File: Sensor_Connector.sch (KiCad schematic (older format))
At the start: 6 parts, among them J3 Sensor_Conn

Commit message: Misc. TODOs
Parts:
- C18, C19: footprint Capacitor_SMD:C_0603_1608Metric_Pad1.05x0.95mm_HandSolder -> Capacitor_SMD:C_0603_1608Metric_Pad1.08x0.95mm_HandSolder
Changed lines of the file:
@@
 $Descr A4 11693 8268
 encoding utf-8
-Sheet 11 13
+Sheet 10 13
 Title "Kleinvoet"
 Date "2020-06-11"
@@
 F 0 "C32" H 3242 5096 50  0000 L CNN
 F 1 "220p" H 3242 5005 50  0000 L CNN
-F 2 "Capacitor_SMD:C_0603_1608Metric_Pad1.05x0.95mm_HandSolder" H 3150 5050 50  0001 C CNN
+F 2 "Capacitor_SMD:C_0603_1608Metric_Pad1.08x0.95mm_HandSolder" H 3150 5050 50  0001 C CNN
 F 3 "~" H 3150 5050 50  0001 C CNN
 F 4 "C0603C221J5GACTU" H 3150 5050 50  0001 C CNN "MPN"
@@
 F 0 "C33" H 3242 4896 50  0000 L CNN
 F 1 "220p" H 3242 4805 50  0000 L CNN
-F 2 "Capacitor_SMD:C_0603_1608Metric_Pad1.05x0.95mm_HandSolder" H 3150 4850 50  0001 C CNN
+F 2 "Capacitor_SMD:C_0603_1608Metric_Pad1.08x0.95mm_HandSolder" H 3150 4850 50  0001 C CNN
 F 3 "~" H 3150 4850 50  0001 C CNN
 F 4 "C0603C221J5GACTU" H 3150 4850 50  0001 C CNN "MPN"

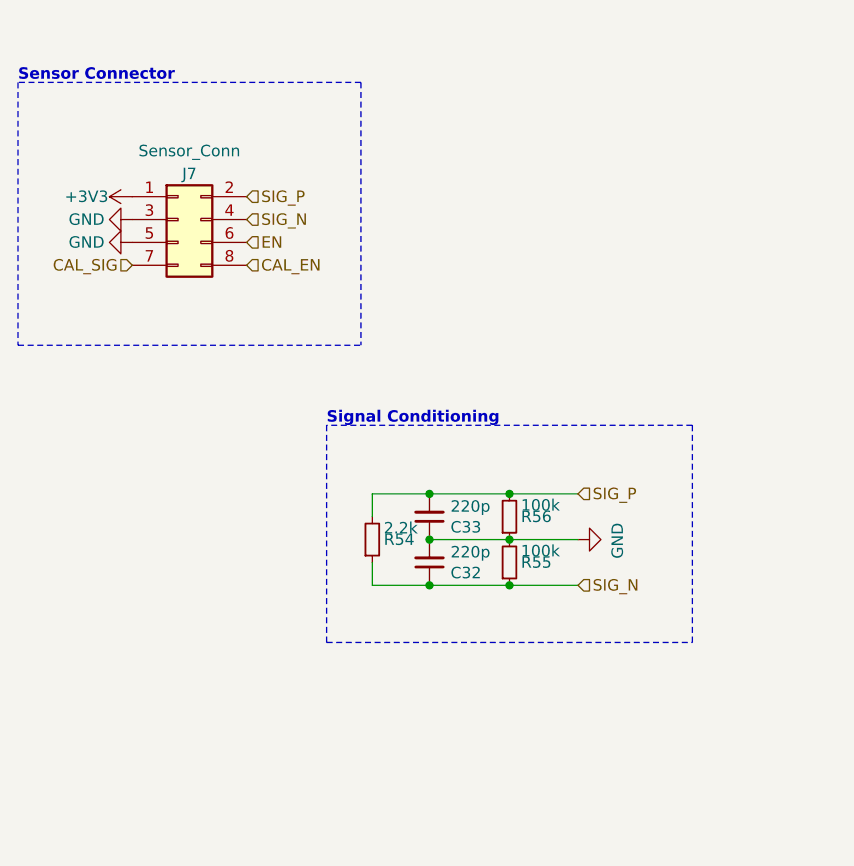
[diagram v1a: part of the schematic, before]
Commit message: Update interface to ADC
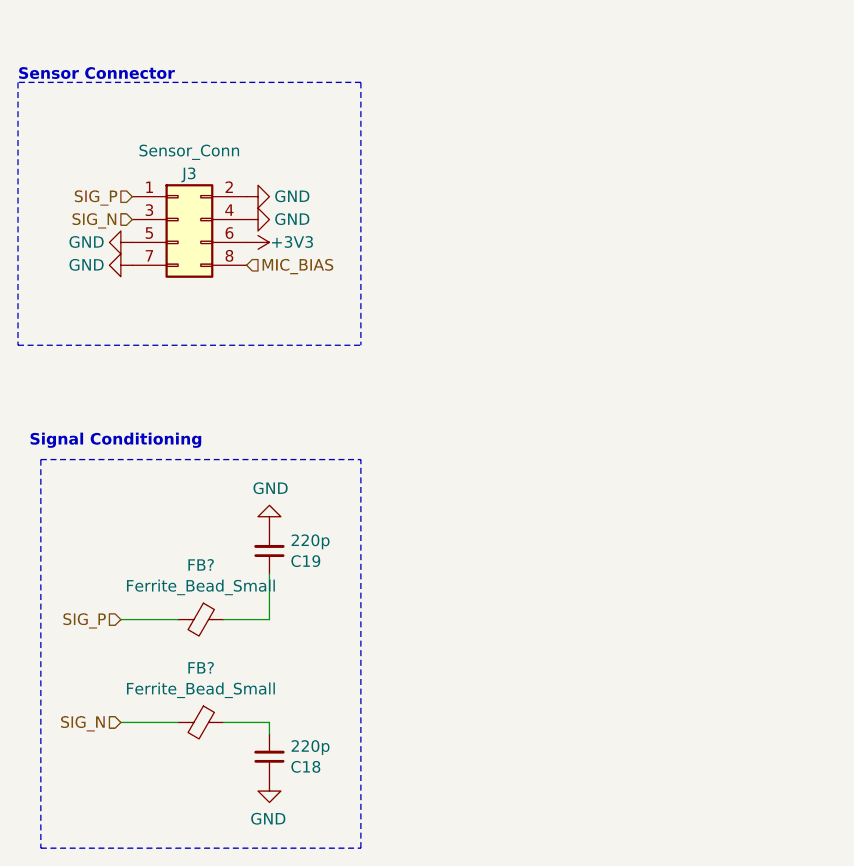
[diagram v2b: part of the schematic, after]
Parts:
- removed R27: 2.2k, Resistor_SMD:R_0603_1608Metric_Pad1.05x0.95mm_HandSolder, symbol Device:R_Small
- removed R28, R29: 100k, Resistor_SMD:R_0603_1608Metric_Pad1.05x0.95mm_HandSolder, symbol Device:R_Small
- added FB? (x2): Ferrite_Bead_Small, symbol Device:Ferrite_Bead_Small
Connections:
- net CAL_SIG is gone; now on net GND: J3.7 (Pin_7)
- net EN is gone; now on net +3V3: J3.6 (Pin_6)
- net +3V3: no longer J3.1 (Pin_1)
- net GND: now also C18.1, C19.2, J3.2 (Pin_2), J3.4 (Pin_4); no longer C18.2, C19.1, J3.3 (Pin_3)
- net SIG_N: now also J3.3 (Pin_3), FB?.2; no longer C18.1, J3.4 (Pin_4)
- net SIG_P: now also J3.1 (Pin_1), FB?.2; no longer C19.2, J3.2 (Pin_2)
- net CAL_EN renamed MIC_BIAS
- new net: C18.2, FB?.1
- new net: C19.1, FB?.1
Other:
- moved on the sheet: C18, C19

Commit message: Add new  ADC module
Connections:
- net GND: no longer J3.7 (Pin_7)
- net MIC_BIAS: no longer names the net of J3.8 (Pin_8)
- no-connect marks 0 -> 2
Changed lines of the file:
@@
 	0    1    -1   0
 $EndComp
-Text HLabel 1850 3550 0    50   Input ~ 0
+Text HLabel 1850 3550 0    50   Output ~ 0
 SIG_N
 $Comp
@@
 	0    1    -1   0
 $EndComp
-Text HLabel 1850 3450 0    50   Input ~ 0
+Text HLabel 1850 3450 0    50   Output ~ 0
 SIG_P
 $Comp
@@
 U 1 1 5F997D5D
 P 2150 5300
+AR Path="/5EE5ECAD/5EE62C2B/5F997D5D" Ref="FB?"  Part="1"
+AR Path="/5EE5ECAD/5EFF163B/5F997D5D" Ref="FB?"  Part="1"
+AR Path="/5EE5ECAD/5EFF6D57/5F997D5D" Ref="FB?"  Part="1"
+AR Path="/5EE5ECAD/5EFFC4F7/5F997D5D" Ref="FB?"  Part="1"
 F 0 "FB?" V 1913 5300 50  0000 C CNN
 F 1 "Ferrite_Bead_Small" V 2004 5300 50  0000 C CNN
@@
 U 1 1 5F999474
 P 2150 5750
+AR Path="/5EE5ECAD/5EE62C2B/5F999474" Ref="FB?"  Part="1"
+AR Path="/5EE5ECAD/5EFF163B/5F999474" Ref="FB?"  Part="1"
+AR Path="/5EE5ECAD/5EFF6D57/5F999474" Ref="FB?"  Part="1"
+AR Path="/5EE5ECAD/5EFFC4F7/5F999474" Ref="FB?"  Part="1"
 F 0 "FB?" V 1913 5750 50  0000 C CNN
 F 1 "Ferrite_Bead_Small" V 2004 5750 50  0000 C CNN
@@
 	1    0    0    -1
 $EndComp
-$Comp
-L power:GND #PWR?
-U 1 1 5F9A5B4F
-P 1850 3750
-AR Path="/5F9A5B4F" Ref="#PWR?"  Part="1"
-AR Path="/5F1E182A/5F9A5B4F" Ref="#PWR?"  Part="1"
-AR Path="/5F27C929/5F9A5B4F" Ref="#PWR?"  Part="1"
-AR Path="/5F2811D8/5F9A5B4F" Ref="#PWR?"  Part="1"
-AR Path="/5F28658C/5F9A5B4F" Ref="#PWR?"  Part="1"
-AR Path="/5F28BBEB/5F9A5B4F" Ref="#PWR?"  Part="1"
-AR Path="/5F29087F/5F9A5B4F" Ref="#PWR?"  Part="1"
-AR Path="/5EE5ECAD/5EE62C2B/5F9A5B4F" Ref="#PWR?"  Part="1"
-AR Path="/5EE5ECAD/5EE62C39/5F9A5B4F" Ref="#PWR?"  Part="1"
-AR Path="/5EE5ECAD/5EE62C47/5F9A5B4F" Ref="#PWR?"  Part="1"
-AR Path="/5EE5ECAD/5EE62C55/5F9A5B4F" Ref="#PWR?"  Part="1"
-AR Path="/5EE5ECAD/5EE8F49C/5F9A5B4F" Ref="#PWR?"  Part="1"
-AR Path="/5EE5ECAD/5EE91C9A/5F9A5B4F" Ref="#PWR?"  Part="1"
-AR Path="/5EE5ECAD/5EE94935/5F9A5B4F" Ref="#PWR?"  Part="1"
-AR Path="/5EE5ECAD/5EE9134C/5F9A5B4F" Ref="#PWR?"  Part="1"
-AR Path="/5EE5ECAD/5EE94699/5F9A5B4F" Ref="#PWR?"  Part="1"
-AR Path="/5EE5ECAD/5EE979DE/5F9A5B4F" Ref="#PWR?"  Part="1"
-AR Path="/5EE5ECAD/5EFF163B/5F9A5B4F" Ref="#PWR?"  Part="1"
-AR Path="/5EE5ECAD/5EFF6D57/5F9A5B4F" Ref="#PWR?"  Part="1"
-AR Path="/5EE5ECAD/5EFFC4F7/5F9A5B4F" Ref="#PWR?"  Part="1"
-F 0 "#PWR?" H 1850 3500 50  0001 C CNN
-F 1 "GND" V 1850 3550 50  0000 C CNN
-F 2 "" H 1850 3750 50  0001 C CNN
-F 3 "" H 1850 3750 50  0001 C CNN
-	1    1850 3750
-	0    1    -1   0
-$EndComp
-Text HLabel 2350 3750 2    50   Input ~ 0
-MIC_BIAS
+NoConn ~ 2350 3750
+NoConn ~ 1850 3750
 $EndSCHEMATC

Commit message: Add SAI & misc.
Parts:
- added TP?: SIG_p, symbol Connector:TestPoint
- added TP?: SIG_N, symbol Connector:TestPoint
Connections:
- net SIG_N: now also TP?.1; no longer J3.3 (Pin_3)
- net SIG_P: now also TP?.1; no longer J3.1 (Pin_1)
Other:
- note added: "(OUT OF DATE!)"
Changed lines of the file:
@@
 	0    1    -1   0
 $EndComp
-Text HLabel 1850 3550 0    50   Output ~ 0
+Text HLabel 4200 3600 0    50   Output ~ 0
 SIG_N
 $Comp
@@
 	0    1    -1   0
 $EndComp
-Text HLabel 1850 3450 0    50   Output ~ 0
+Text HLabel 4200 3350 0    50   Output ~ 0
 SIG_P
 $Comp
@@
 NoConn ~ 2350 3750
 NoConn ~ 1850 3750
+$Comp
+L Connector:TestPoint TP?
+U 1 1 5FC79004
+P 4200 3350
+F 0 "TP?" V 4154 3538 50  0000 L CNN
+F 1 "SIG_p" V 4245 3538 50  0000 L CNN
+F 2 "" H 4400 3350 50  0001 C CNN
+F 3 "~" H 4400 3350 50  0001 C CNN
+	1    4200 3350
+	0    1    1    0
+$EndComp
+$Comp
+L Connector:TestPoint TP?
+U 1 1 5FC7A09A
+P 4200 3600
+F 0 "TP?" V 4154 3788 50  0000 L CNN
+F 1 "SIG_N" V 4245 3788 50  0000 L CNN
+F 2 "" H 4400 3600 50  0001 C CNN
+F 3 "~" H 4400 3600 50  0001 C CNN
+	1    4200 3600
+	0    1    1    0
+$EndComp
+Text Notes 7600 1450 0    100  ~ 20
+(OUT OF DATE!)
 $EndSCHEMATC

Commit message: Assign footprints
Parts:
- removed TP?: SIG_p, symbol Connector:TestPoint
- removed TP?: SIG_N, symbol Connector:TestPoint
- added TP19: SIG, TestPoint:TestPoint_2Pads_Pitch2.54mm_Drill0.8mm, symbol Connector:TestPoint_2Pole
- FB3, FB4: renamed from FB?; footprint (none) -> Inductor_SMD:L_0603_1608Metric_Pad1.05x0.95mm_HandSolder
- J3: footprint Connector_PinHeader_2.00mm:PinHeader_2x04_P2.00mm_Vertical -> grootvoet:TE_7-215079-8
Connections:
- net SIG_N: now also TP19.1
- net SIG_P: now also TP19.2
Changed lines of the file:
@@
 $Descr A4 11693 8268
 encoding utf-8
-Sheet 7 13
+Sheet 10 9
 Title "Kleinvoet"
 Date "2020-06-11"
@@
 AR Path="/5EE5ECAD/5EFF6D57/5EEA2252" Ref="C30"  Part="1"
 AR Path="/5EE5ECAD/5EFFC4F7/5EEA2252" Ref="C32"  Part="1"
-F 0 "C18" H 2542 5946 50  0000 L CNN
+F 0 "C32" H 2542 5946 50  0000 L CNN
 F 1 "220p" H 2542 5855 50  0000 L CNN
 F 2 "Capacitor_SMD:C_0603_1608Metric_Pad1.08x0.95mm_HandSolder" H 2450 5900 50  0001 C CNN
@@
 AR Path="/5EE5ECAD/5EFF6D57/5EEA248A" Ref="C31"  Part="1"
 AR Path="/5EE5ECAD/5EFFC4F7/5EEA248A" Ref="C33"  Part="1"
-F 0 "C19" H 2542 5046 50  0000 L CNN
+F 0 "C33" H 2542 5046 50  0000 L CNN
 F 1 "220p" H 2542 4955 50  0000 L CNN
 F 2 "Capacitor_SMD:C_0603_1608Metric_Pad1.08x0.95mm_HandSolder" H 2450 5000 50  0001 C CNN
@@
 AR Path="/5EE5ECAD/5EFF6D57/5EFE739C" Ref="#PWR079"  Part="1"
 AR Path="/5EE5ECAD/5EFFC4F7/5EFE739C" Ref="#PWR085"  Part="1"
-F 0 "#PWR067" H 1850 3400 50  0001 C CNN
+F 0 "#PWR085" H 1850 3400 50  0001 C CNN
 F 1 "GND" V 1850 3450 50  0000 C CNN
 F 2 "" H 1850 3650 50  0001 C CNN
@@
 	0    1    -1   0
 $EndComp
-Text HLabel 4200 3600 0    50   Output ~ 0
+Text HLabel 4050 4000 0    50   Output ~ 0
 SIG_N
 $Comp
@@
 AR Path="/5EE5ECAD/5EFF6D57/5EE5C6A5" Ref="#PWR077"  Part="1"
 AR Path="/5EE5ECAD/5EFFC4F7/5EE5C6A5" Ref="#PWR083"  Part="1"
-F 0 "#PWR065" H 2350 3500 50  0001 C CNN
+F 0 "#PWR083" H 2350 3500 50  0001 C CNN
 F 1 "+3V3" V 2350 3850 50  0000 C CNN
 F 2 "" H 2350 3650 50  0001 C CNN
@@
 	0    1    -1   0
 $EndComp
-Text HLabel 4200 3350 0    50   Output ~ 0
+Text HLabel 4450 4000 2    50   Output ~ 0
 SIG_P
 $Comp
@@
 AR Path="/5EE5ECAD/5EFF6D57/5EF00E56" Ref="#PWR0146"  Part="1"
 AR Path="/5EE5ECAD/5EFFC4F7/5EF00E56" Ref="#PWR0147"  Part="1"
-F 0 "#PWR0144" H 2350 3200 50  0001 C CNN
+F 0 "#PWR0147" H 2350 3200 50  0001 C CNN
 F 1 "GND" V 2350 3250 50  0000 C CNN
 F 2 "" H 2350 3450 50  0001 C CNN
@@
 $EndComp
 $Comp
-L Device:Ferrite_Bead_Small FB?
+L Device:Ferrite_Bead_Small FB3
 U 1 1 5F997D5D
 P 2150 5300
-AR Path="/5EE5ECAD/5EE62C2B/5F997D5D" Ref="FB?"  Part="1"
-AR Path="/5EE5ECAD/5EFF163B/5F997D5D" Ref="FB?"  Part="1"
-AR Path="/5EE5ECAD/5EFF6D57/5F997D5D" Ref="FB?"  Part="1"
-AR Path="/5EE5ECAD/5EFFC4F7/5F997D5D" Ref="FB?"  Part="1"
-F 0 "FB?" V 1913 5300 50  0000 C CNN
+AR Path="/5EE5ECAD/5EE62C2B/5F997D5D" Ref="FB3"  Part="1"
+AR Path="/5EE5ECAD/5EFF163B/5F997D5D" Ref="FB5"  Part="1"
+AR Path="/5EE5ECAD/5EFF6D57/5F997D5D" Ref="FB7"  Part="1"
+AR Path="/5EE5ECAD/5EFFC4F7/5F997D5D" Ref="FB12"  Part="1"
+F 0 "FB12" V 1913 5300 50  0000 C CNN
 F 1 "Ferrite_Bead_Small" V 2004 5300 50  0000 C CNN
-F 2 "" V 2080 5300 50  0001 C CNN
+F 2 "Inductor_SMD:L_0603_1608Metric_Pad1.05x0.95mm_HandSolder" V 2080 5300 50  0001 C CNN
 F 3 "~" H 2150 5300 50  0001 C CNN
 	1    2150 5300
@@
 $EndComp
 $Comp
-L Device:Ferrite_Bead_Small FB?
+L Device:Ferrite_Bead_Small FB4
 U 1 1 5F999474
 P 2150 5750
-AR Path="/5EE5ECAD/5EE62C2B/5F999474" Ref="FB?"  Part="1"
-AR Path="/5EE5ECAD/5EFF163B/5F999474" Ref="FB?"  Part="1"
-AR Path="/5EE5ECAD/5EFF6D57/5F999474" Ref="FB?"  Part="1"
-AR Path="/5EE5ECAD/5EFFC4F7/5F999474" Ref="FB?"  Part="1"
-F 0 "FB?" V 1913 5750 50  0000 C CNN
+AR Path="/5EE5ECAD/5EE62C2B/5F999474" Ref="FB4"  Part="1"
+AR Path="/5EE5ECAD/5EFF163B/5F999474" Ref="FB6"  Part="1"
+AR Path="/5EE5ECAD/5EFF6D57/5F999474" Ref="FB11"  Part="1"
+AR Path="/5EE5ECAD/5EFFC4F7/5F999474" Ref="FB13"  Part="1"
+F 0 "FB13" V 1913 5750 50  0000 C CNN
 F 1 "Ferrite_Bead_Small" V 2004 5750 50  0000 C CNN
-F 2 "" V 2080 5750 50  0001 C CNN
+F 2 "Inductor_SMD:L_0603_1608Metric_Pad1.05x0.95mm_HandSolder" V 2080 5750 50  0001 C CNN
 F 3 "~" H 2150 5750 50  0001 C CNN
 	1    2150 5750
@@
 AR Path="/5EE5ECAD/5EFF6D57/5EEA4A0A" Ref="#PWR080"  Part="1"
 AR Path="/5EE5ECAD/5EFFC4F7/5EEA4A0A" Ref="#PWR086"  Part="1"
-F 0 "#PWR068" H 2450 5750 50  0001 C CNN
+F 0 "#PWR086" H 2450 5750 50  0001 C CNN
 F 1 "GND" H 2455 5827 50  0000 C CNN
 F 2 "" H 2450 6000 50  0001 C CNN
@@
 AR Path="/5F28BBEB/5F99FD60" Ref="#PWR?"  Part="1"
 AR Path="/5F29087F/5F99FD60" Ref="#PWR?"  Part="1"
-AR Path="/5EE5ECAD/5EE62C2B/5F99FD60" Ref="#PWR?"  Part="1"
+AR Path="/5EE5ECAD/5EE62C2B/5F99FD60" Ref="#PWR0185"  Part="1"
 AR Path="/5EE5ECAD/5EE62C39/5F99FD60" Ref="#PWR?"  Part="1"
 AR Path="/5EE5ECAD/5EE62C47/5F99FD60" Ref="#PWR?"  Part="1"
@@
 AR Path="/5EE5ECAD/5EE94699/5F99FD60" Ref="#PWR?"  Part="1"
 AR Path="/5EE5ECAD/5EE979DE/5F99FD60" Ref="#PWR?"  Part="1"
-AR Path="/5EE5ECAD/5EFF163B/5F99FD60" Ref="#PWR?"  Part="1"
-AR Path="/5EE5ECAD/5EFF6D57/5F99FD60" Ref="#PWR?"  Part="1"
-AR Path="/5EE5ECAD/5EFFC4F7/5F99FD60" Ref="#PWR?"  Part="1"
-F 0 "#PWR?" H 2450 4650 50  0001 C CNN
+AR Path="/5EE5ECAD/5EFF163B/5F99FD60" Ref="#PWR0187"  Part="1"
+AR Path="/5EE5ECAD/5EFF6D57/5F99FD60" Ref="#PWR0189"  Part="1"
+AR Path="/5EE5ECAD/5EFFC4F7/5F99FD60" Ref="#PWR0191"  Part="1"
+F 0 "#PWR0191" H 2450 4650 50  0001 C CNN
 F 1 "GND" H 2455 4727 50  0000 C CNN
 F 2 "" H 2450 4900 50  0001 C CNN
@@
 AR Path="/5F28BBEB/5F9A54A7" Ref="#PWR?"  Part="1"
 AR Path="/5F29087F/5F9A54A7" Ref="#PWR?"  Part="1"
-AR Path="/5EE5ECAD/5EE62C2B/5F9A54A7" Ref="#PWR?"  Part="1"
+AR Path="/5EE5ECAD/5EE62C2B/5F9A54A7" Ref="#PWR0184"  Part="1"
 AR Path="/5EE5ECAD/5EE62C39/5F9A54A7" Ref="#PWR?"  Part="1"
 AR Path="/5EE5ECAD/5EE62C47/5F9A54A7" Ref="#PWR?"  Part="1"
@@
 AR Path="/5EE5ECAD/5EE94699/5F9A54A7" Ref="#PWR?"  Part="1"
 AR Path="/5EE5ECAD/5EE979DE/5F9A54A7" Ref="#PWR?"  Part="1"
-AR Path="/5EE5ECAD/5EFF163B/5F9A54A7" Ref="#PWR?"  Part="1"
-AR Path="/5EE5ECAD/5EFF6D57/5F9A54A7" Ref="#PWR?"  Part="1"
-AR Path="/5EE5ECAD/5EFFC4F7/5F9A54A7" Ref="#PWR?"  Part="1"
-F 0 "#PWR?" H 2350 3300 50  0001 C CNN
+AR Path="/5EE5ECAD/5EFF163B/5F9A54A7" Ref="#PWR0186"  Part="1"
+AR Path="/5EE5ECAD/5EFF6D57/5F9A54A7" Ref="#PWR0188"  Part="1"
+AR Path="/5EE5ECAD/5EFFC4F7/5F9A54A7" Ref="#PWR0190"  Part="1"
+F 0 "#PWR0190" H 2350 3300 50  0001 C CNN
 F 1 "GND" V 2350 3350 50  0000 C CNN
 F 2 "" H 2350 3550 50  0001 C CNN
@@
 AR Path="/5EE5ECAD/5EFF6D57/5EDAD860" Ref="J6"  Part="1"
 AR Path="/5EE5ECAD/5EFFC4F7/5EDAD860" Ref="J7"  Part="1"
-F 0 "J3" H 2100 3750 50  0000 C CNN
+F 0 "J7" H 2100 3750 50  0000 C CNN
 F 1 "Sensor_Conn" H 2100 3850 50  0000 C CNN
-F 2 "Connector_PinHeader_2.00mm:PinHeader_2x04_P2.00mm_Vertical" H 2050 3550 50  0001 C CNN
+F 2 "grootvoet:TE_7-215079-8" H 2050 3550 50  0001 C CNN
 F 3 "~" H 2050 3550 50  0001 C CNN
 F 4 "" H 2050 3550 50  0001 C CNN "MPN"
@@
 NoConn ~ 2350 3750
 NoConn ~ 1850 3750
-$Comp
-L Connector:TestPoint TP?
-U 1 1 5FC79004
-P 4200 3350
-F 0 "TP?" V 4154 3538 50  0000 L CNN
-F 1 "SIG_p" V 4245 3538 50  0000 L CNN
-F 2 "" H 4400 3350 50  0001 C CNN
-F 3 "~" H 4400 3350 50  0001 C CNN
-	1    4200 3350
-	0    1    1    0
-$EndComp
-$Comp
-L Connector:TestPoint TP?
-U 1 1 5FC7A09A
-P 4200 3600
-F 0 "TP?" V 4154 3788 50  0000 L CNN
-F 1 "SIG_N" V 4245 3788 50  0000 L CNN
-F 2 "" H 4400 3600 50  0001 C CNN
-F 3 "~" H 4400 3600 50  0001 C CNN
-	1    4200 3600
-	0    1    1    0
-$EndComp
 Text Notes 7600 1450 0    100  ~ 20
 (OUT OF DATE!)
+$Comp
+L Connector:TestPoint_2Pole TP19
+U 1 1 5F9E0F6D
+P 4250 4000
+AR Path="/5EE5ECAD/5EE62C2B/5F9E0F6D" Ref="TP19"  Part="1"
+AR Path="/5EE5ECAD/5EFF163B/5F9E0F6D" Ref="TP20"  Part="1"
+AR Path="/5EE5ECAD/5EFF6D57/5F9E0F6D" Ref="TP21"  Part="1"
+AR Path="/5EE5ECAD/5EFFC4F7/5F9E0F6D" Ref="TP22"  Part="1"
+F 0 "TP22" H 4250 4195 50  0000 C CNN
+F 1 "SIG" H 4250 4104 50  0000 C CNN
+F 2 "TestPoint:TestPoint_2Pads_Pitch2.54mm_Drill0.8mm" H 4250 4000 50  0001 C CNN
+F 3 "~" H 4250 4000 50  0001 C CNN
+	1    4250 4000
+	1    0    0    -1
+$EndComp
 $EndSCHEMATC

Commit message: Import to PCB
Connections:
- net SIG_N: now also J3.3 (Pin_3)
- net SIG_P: now also J3.1 (Pin_1)
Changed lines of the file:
@@
 $Descr A4 11693 8268
 encoding utf-8
-Sheet 10 9
+Sheet 5 9
 Title "Kleinvoet"
 Date "2020-06-11"
@@
 AR Path="/5EE5ECAD/5EFF6D57/5EEA2252" Ref="C30"  Part="1"
 AR Path="/5EE5ECAD/5EFFC4F7/5EEA2252" Ref="C32"  Part="1"
-F 0 "C32" H 2542 5946 50  0000 L CNN
+F 0 "C18" H 2542 5946 50  0000 L CNN
 F 1 "220p" H 2542 5855 50  0000 L CNN
 F 2 "Capacitor_SMD:C_0603_1608Metric_Pad1.08x0.95mm_HandSolder" H 2450 5900 50  0001 C CNN
@@
 AR Path="/5EE5ECAD/5EFF6D57/5EEA248A" Ref="C31"  Part="1"
 AR Path="/5EE5ECAD/5EFFC4F7/5EEA248A" Ref="C33"  Part="1"
-F 0 "C33" H 2542 5046 50  0000 L CNN
+F 0 "C19" H 2542 5046 50  0000 L CNN
 F 1 "220p" H 2542 4955 50  0000 L CNN
 F 2 "Capacitor_SMD:C_0603_1608Metric_Pad1.08x0.95mm_HandSolder" H 2450 5000 50  0001 C CNN
@@
 AR Path="/5EE5ECAD/5EFF6D57/5EFE739C" Ref="#PWR079"  Part="1"
 AR Path="/5EE5ECAD/5EFFC4F7/5EFE739C" Ref="#PWR085"  Part="1"
-F 0 "#PWR085" H 1850 3400 50  0001 C CNN
+F 0 "#PWR079" H 1850 3400 50  0001 C CNN
 F 1 "GND" V 1850 3450 50  0000 C CNN
 F 2 "" H 1850 3650 50  0001 C CNN
@@
 AR Path="/5EE5ECAD/5EFF6D57/5EE5C6A5" Ref="#PWR077"  Part="1"
 AR Path="/5EE5ECAD/5EFFC4F7/5EE5C6A5" Ref="#PWR083"  Part="1"
-F 0 "#PWR083" H 2350 3500 50  0001 C CNN
+F 0 "#PWR077" H 2350 3500 50  0001 C CNN
 F 1 "+3V3" V 2350 3850 50  0000 C CNN
 F 2 "" H 2350 3650 50  0001 C CNN
@@
 AR Path="/5EE5ECAD/5EFF6D57/5EF00E56" Ref="#PWR0146"  Part="1"
 AR Path="/5EE5ECAD/5EFFC4F7/5EF00E56" Ref="#PWR0147"  Part="1"
-F 0 "#PWR0147" H 2350 3200 50  0001 C CNN
+F 0 "#PWR0146" H 2350 3200 50  0001 C CNN
 F 1 "GND" V 2350 3250 50  0000 C CNN
 F 2 "" H 2350 3450 50  0001 C CNN
@@
 AR Path="/5EE5ECAD/5EFF6D57/5F997D5D" Ref="FB7"  Part="1"
 AR Path="/5EE5ECAD/5EFFC4F7/5F997D5D" Ref="FB12"  Part="1"
-F 0 "FB12" V 1913 5300 50  0000 C CNN
+F 0 "FB3" V 1913 5300 50  0000 C CNN
 F 1 "Ferrite_Bead_Small" V 2004 5300 50  0000 C CNN
 F 2 "Inductor_SMD:L_0603_1608Metric_Pad1.05x0.95mm_HandSolder" V 2080 5300 50  0001 C CNN
@@
 AR Path="/5EE5ECAD/5EFF6D57/5F999474" Ref="FB11"  Part="1"
 AR Path="/5EE5ECAD/5EFFC4F7/5F999474" Ref="FB13"  Part="1"
-F 0 "FB13" V 1913 5750 50  0000 C CNN
+F 0 "FB4" V 1913 5750 50  0000 C CNN
 F 1 "Ferrite_Bead_Small" V 2004 5750 50  0000 C CNN
 F 2 "Inductor_SMD:L_0603_1608Metric_Pad1.05x0.95mm_HandSolder" V 2080 5750 50  0001 C CNN
@@
 AR Path="/5EE5ECAD/5EFF6D57/5EEA4A0A" Ref="#PWR080"  Part="1"
 AR Path="/5EE5ECAD/5EFFC4F7/5EEA4A0A" Ref="#PWR086"  Part="1"
-F 0 "#PWR086" H 2450 5750 50  0001 C CNN
+F 0 "#PWR080" H 2450 5750 50  0001 C CNN
 F 1 "GND" H 2455 5827 50  0000 C CNN
 F 2 "" H 2450 6000 50  0001 C CNN
@@
 AR Path="/5EE5ECAD/5EFF6D57/5F99FD60" Ref="#PWR0189"  Part="1"
 AR Path="/5EE5ECAD/5EFFC4F7/5F99FD60" Ref="#PWR0191"  Part="1"
-F 0 "#PWR0191" H 2450 4650 50  0001 C CNN
+F 0 "#PWR0189" H 2450 4650 50  0001 C CNN
 F 1 "GND" H 2455 4727 50  0000 C CNN
 F 2 "" H 2450 4900 50  0001 C CNN
@@
 AR Path="/5EE5ECAD/5EFF6D57/5F9A54A7" Ref="#PWR0188"  Part="1"
 AR Path="/5EE5ECAD/5EFFC4F7/5F9A54A7" Ref="#PWR0190"  Part="1"
-F 0 "#PWR0190" H 2350 3300 50  0001 C CNN
+F 0 "#PWR0188" H 2350 3300 50  0001 C CNN
 F 1 "GND" V 2350 3350 50  0000 C CNN
 F 2 "" H 2350 3550 50  0001 C CNN
@@
 AR Path="/5EE5ECAD/5EFF6D57/5EDAD860" Ref="J6"  Part="1"
 AR Path="/5EE5ECAD/5EFFC4F7/5EDAD860" Ref="J7"  Part="1"
-F 0 "J7" H 2100 3750 50  0000 C CNN
+F 0 "J3" H 2100 3750 50  0000 C CNN
 F 1 "Sensor_Conn" H 2100 3850 50  0000 C CNN
 F 2 "grootvoet:TE_7-215079-8" H 2050 3550 50  0001 C CNN
@@
 AR Path="/5EE5ECAD/5EFF6D57/5F9E0F6D" Ref="TP21"  Part="1"
 AR Path="/5EE5ECAD/5EFFC4F7/5F9E0F6D" Ref="TP22"  Part="1"
-F 0 "TP22" H 4250 4195 50  0000 C CNN
+F 0 "TP19" H 4250 4195 50  0000 C CNN
 F 1 "SIG" H 4250 4104 50  0000 C CNN
 F 2 "TestPoint:TestPoint_2Pads_Pitch2.54mm_Drill0.8mm" H 4250 4000 50  0001 C CNN
@@
 	1    0    0    -1
 $EndComp
+Text HLabel 1850 3550 0    50   Output ~ 0
+SIG_N
+Text HLabel 1850 3450 0    50   Output ~ 0
+SIG_P
 $EndSCHEMATC

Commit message: Update to TRAX tolerances
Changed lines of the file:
@@
 $Descr A4 11693 8268
 encoding utf-8
-Sheet 5 9
+Sheet 6 9
 Title "Kleinvoet"
 Date "2020-06-11"
@@
 AR Path="/5EE5ECAD/5EFF6D57/5EEA2252" Ref="C30"  Part="1"
 AR Path="/5EE5ECAD/5EFFC4F7/5EEA2252" Ref="C32"  Part="1"
-F 0 "C18" H 2542 5946 50  0000 L CNN
+F 0 "C30" H 2542 5946 50  0000 L CNN
 F 1 "220p" H 2542 5855 50  0000 L CNN
 F 2 "Capacitor_SMD:C_0603_1608Metric_Pad1.08x0.95mm_HandSolder" H 2450 5900 50  0001 C CNN
@@
 AR Path="/5EE5ECAD/5EFF6D57/5EEA248A" Ref="C31"  Part="1"
 AR Path="/5EE5ECAD/5EFFC4F7/5EEA248A" Ref="C33"  Part="1"
-F 0 "C19" H 2542 5046 50  0000 L CNN
+F 0 "C31" H 2542 5046 50  0000 L CNN
 F 1 "220p" H 2542 4955 50  0000 L CNN
 F 2 "Capacitor_SMD:C_0603_1608Metric_Pad1.08x0.95mm_HandSolder" H 2450 5000 50  0001 C CNN
@@
 AR Path="/5EE5ECAD/5EFF6D57/5F997D5D" Ref="FB7"  Part="1"
 AR Path="/5EE5ECAD/5EFFC4F7/5F997D5D" Ref="FB12"  Part="1"
-F 0 "FB3" V 1913 5300 50  0000 C CNN
+F 0 "FB7" V 1913 5300 50  0000 C CNN
 F 1 "Ferrite_Bead_Small" V 2004 5300 50  0000 C CNN
 F 2 "Inductor_SMD:L_0603_1608Metric_Pad1.05x0.95mm_HandSolder" V 2080 5300 50  0001 C CNN
@@
 AR Path="/5EE5ECAD/5EFF6D57/5F999474" Ref="FB11"  Part="1"
 AR Path="/5EE5ECAD/5EFFC4F7/5F999474" Ref="FB13"  Part="1"
-F 0 "FB4" V 1913 5750 50  0000 C CNN
+F 0 "FB11" V 1913 5750 50  0000 C CNN
 F 1 "Ferrite_Bead_Small" V 2004 5750 50  0000 C CNN
 F 2 "Inductor_SMD:L_0603_1608Metric_Pad1.05x0.95mm_HandSolder" V 2080 5750 50  0001 C CNN
@@
 AR Path="/5EE5ECAD/5EFF6D57/5EDAD860" Ref="J6"  Part="1"
 AR Path="/5EE5ECAD/5EFFC4F7/5EDAD860" Ref="J7"  Part="1"
-F 0 "J3" H 2100 3750 50  0000 C CNN
+F 0 "J6" H 2100 3750 50  0000 C CNN
 F 1 "Sensor_Conn" H 2100 3850 50  0000 C CNN
 F 2 "grootvoet:TE_7-215079-8" H 2050 3550 50  0001 C CNN
@@
 AR Path="/5EE5ECAD/5EFF6D57/5F9E0F6D" Ref="TP21"  Part="1"
 AR Path="/5EE5ECAD/5EFFC4F7/5F9E0F6D" Ref="TP22"  Part="1"
-F 0 "TP19" H 4250 4195 50  0000 C CNN
+F 0 "TP21" H 4250 4195 50  0000 C CNN
 F 1 "SIG" H 4250 4104 50  0000 C CNN
 F 2 "TestPoint:TestPoint_2Pads_Pitch2.54mm_Drill0.8mm" H 4250 4000 50  0001 C CNN
